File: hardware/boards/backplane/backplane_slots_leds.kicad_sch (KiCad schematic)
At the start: 16 parts, among them J10 I2C_IN, J11 I2C_OUT, J12 LED_EXT_OUT, J14 DC_IN, J15 DC_OUT, J8 LED_EXT_IN

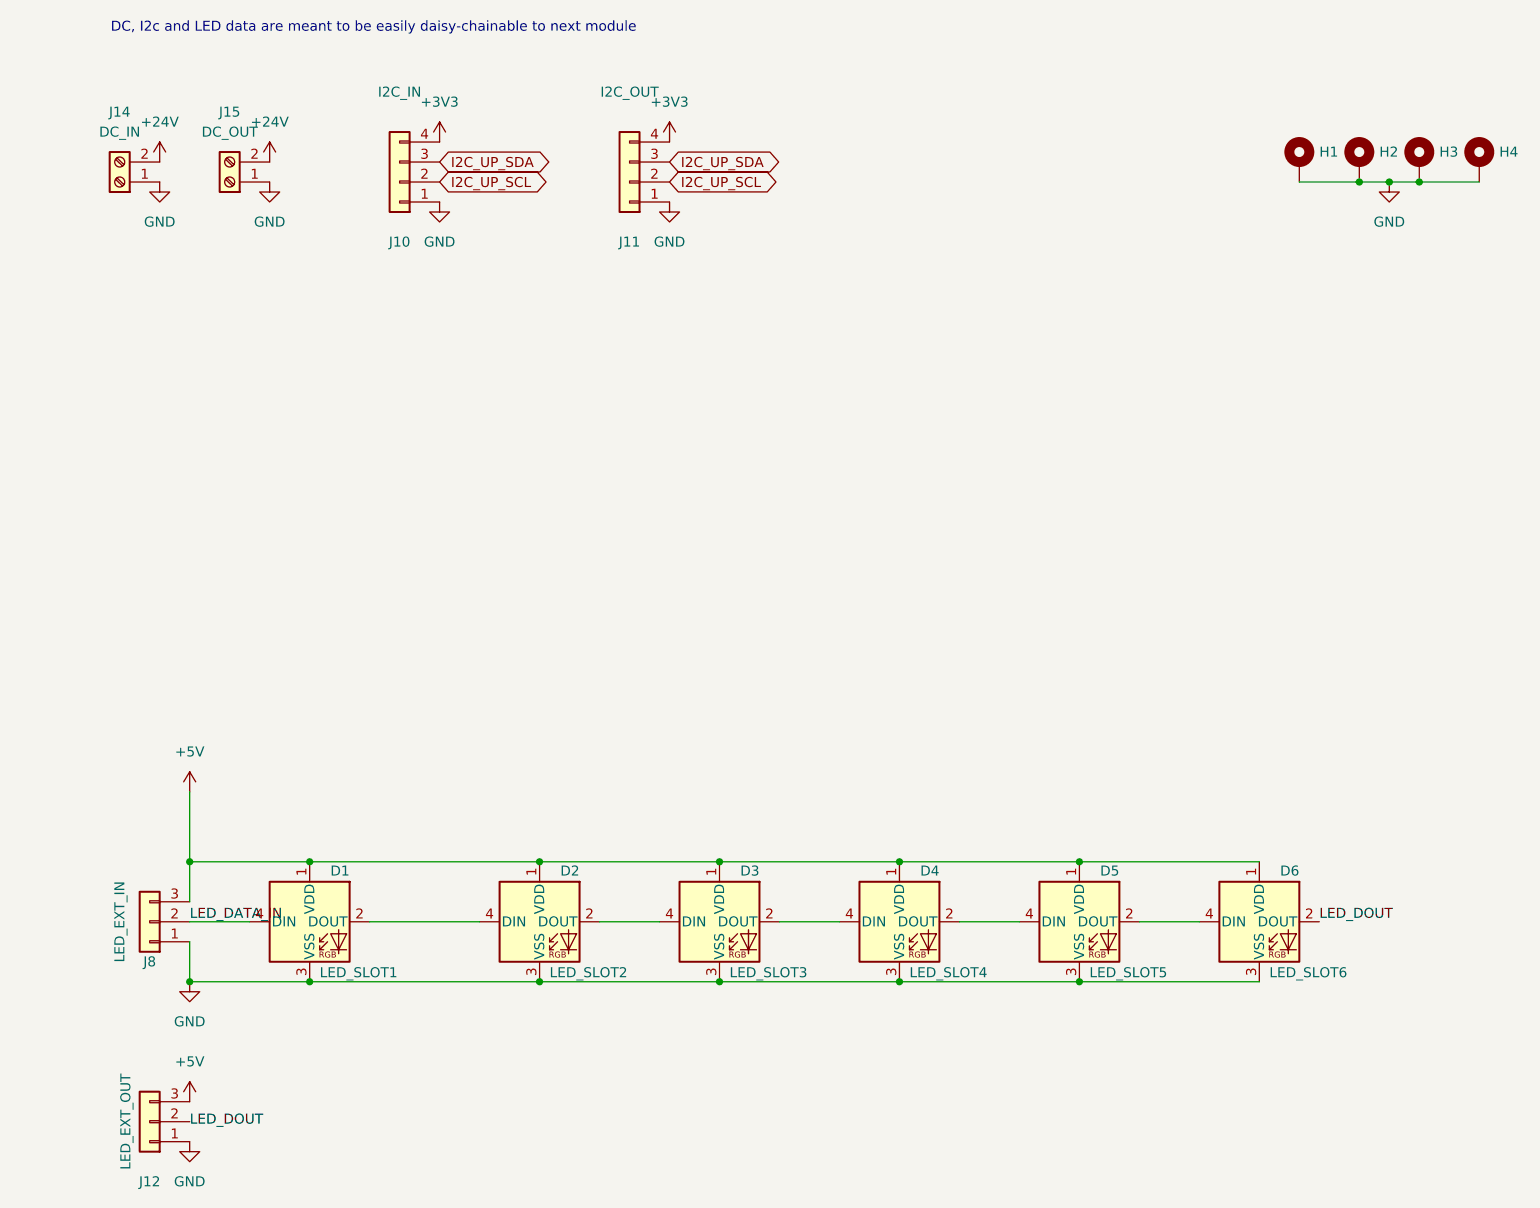
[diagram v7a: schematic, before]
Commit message: Add adjustable DC-DC module to backplane
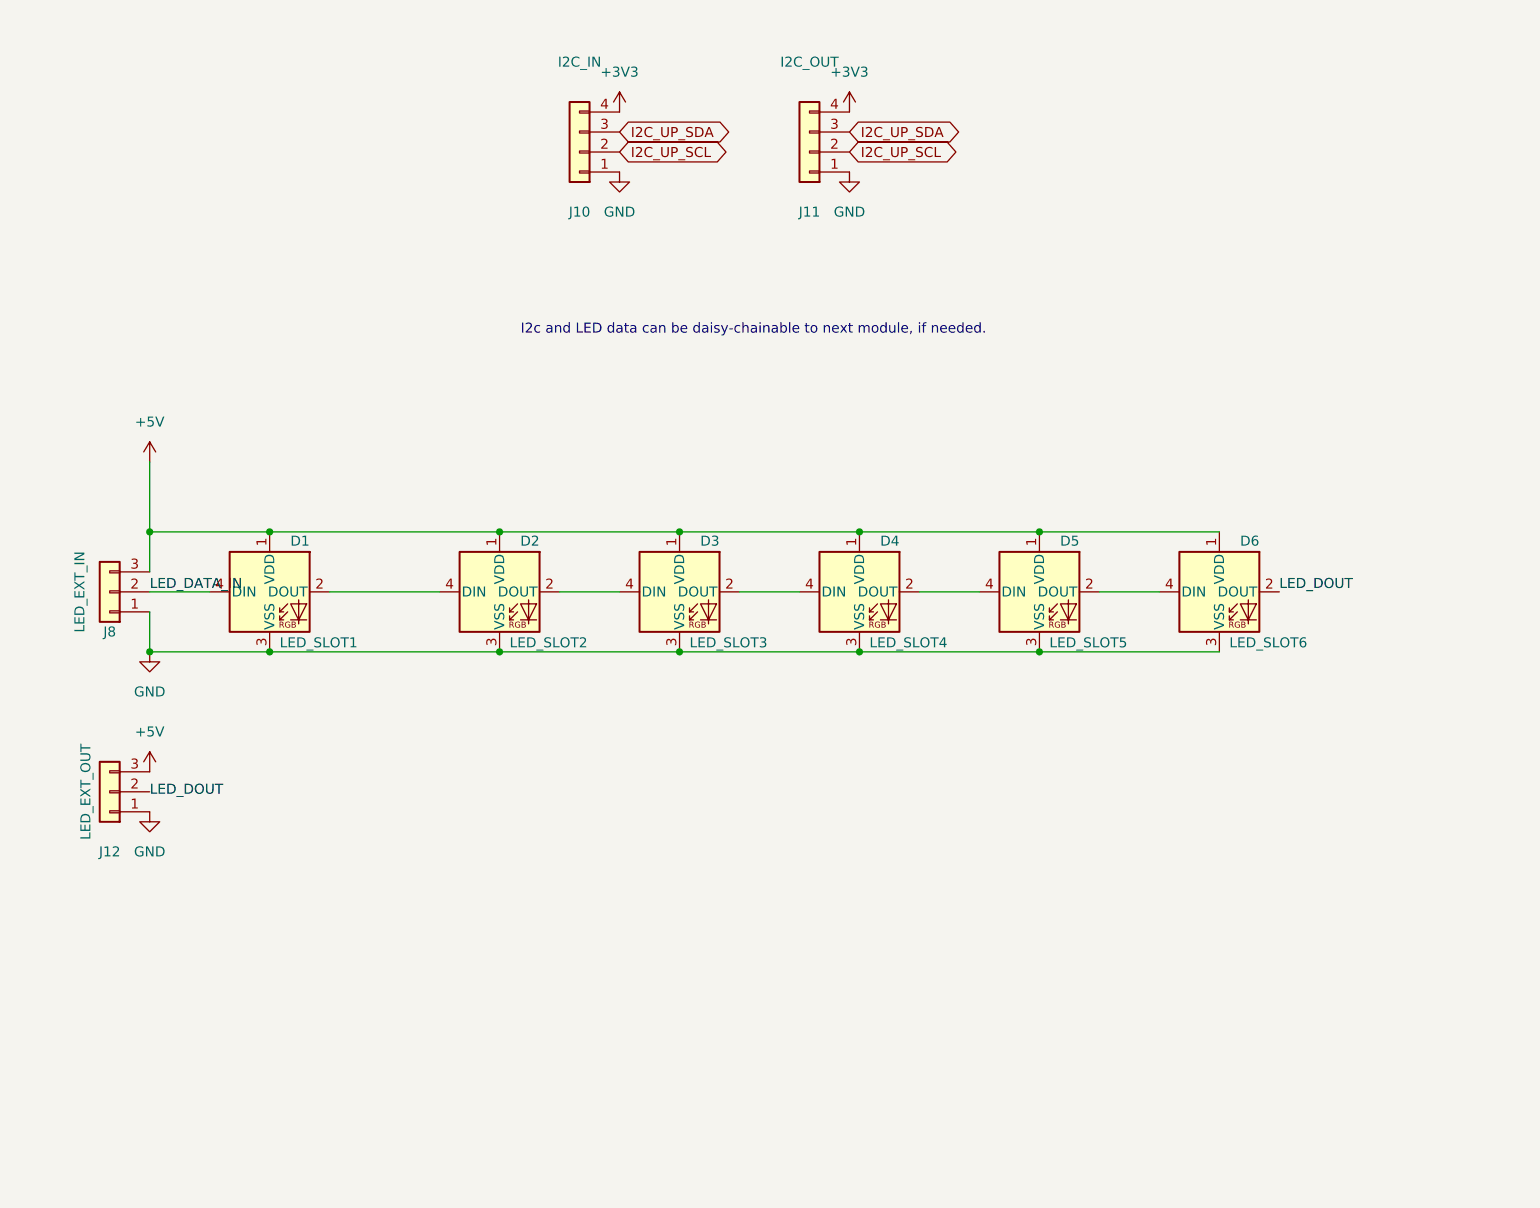
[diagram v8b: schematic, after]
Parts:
- removed H1, H2, H3, H4: MountingHole_Pad, MountingHole:MountingHole_3.2mm_M3_Pad_Via, symbol Mechanical:MountingHole_Pad
- removed J14: DC_IN, mini-rack-power:DEGSON_DG135T-10.16-02P, symbol Connector:Screw_Terminal_01x02
- removed J15: DC_OUT, mini-rack-power:DEGSON_DG135T-10.16-02P, symbol Connector:Screw_Terminal_01x02
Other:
- note added: "I2c and LED data can be daisy-chainable to next module, if needed."
- note removed: "DC, I2c and LED data are meant to be easily daisy-chainable to next module"
- moved on the sheet: D1, D2, D3, D4, D5, D6, J10, J11, J12, J8
